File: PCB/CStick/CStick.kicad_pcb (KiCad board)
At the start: 2 copper layers, 39.1 x 31.5 mm, 6 parts, among them J1 Conn_01x04_Male, U1 Stickbox_Assembly

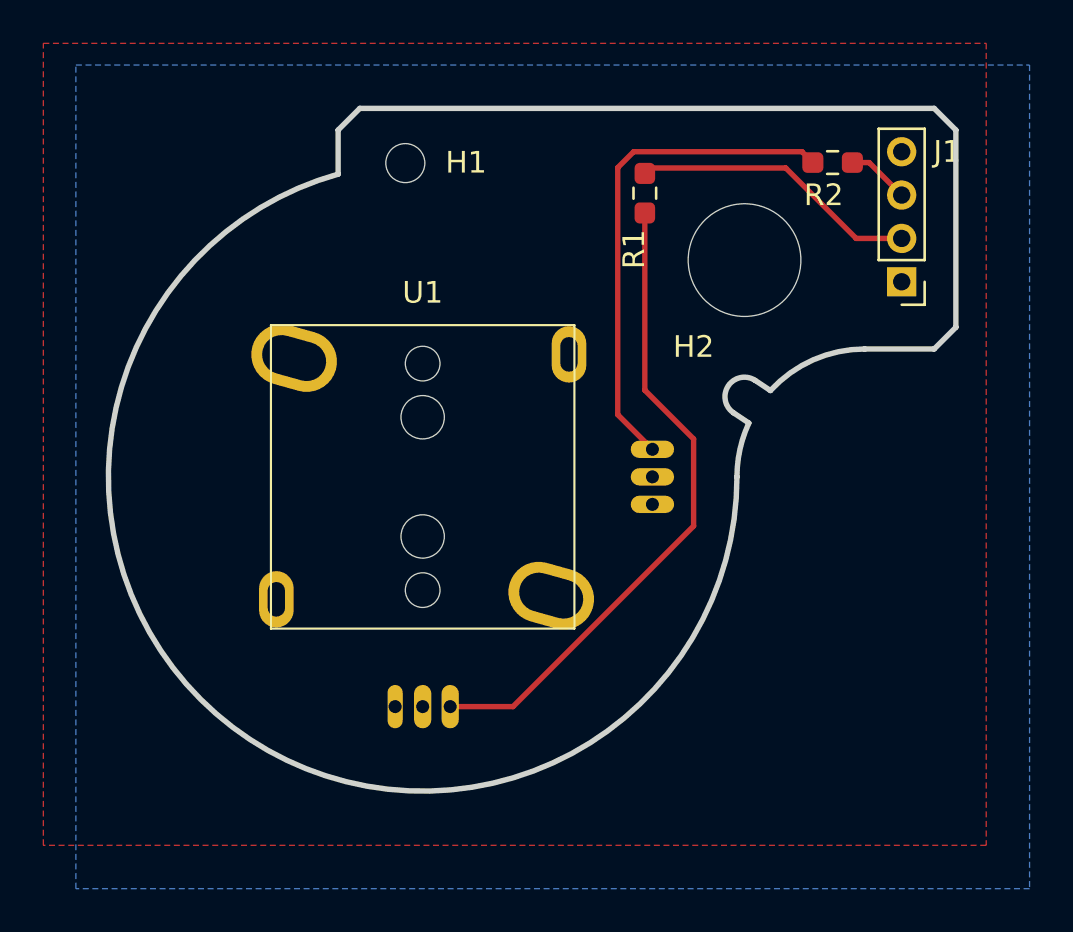
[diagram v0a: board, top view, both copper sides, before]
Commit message: Changed PCB folder structure to sperate Motherboard from Cstick board, updated the diode part number for JLC to one that is in stock
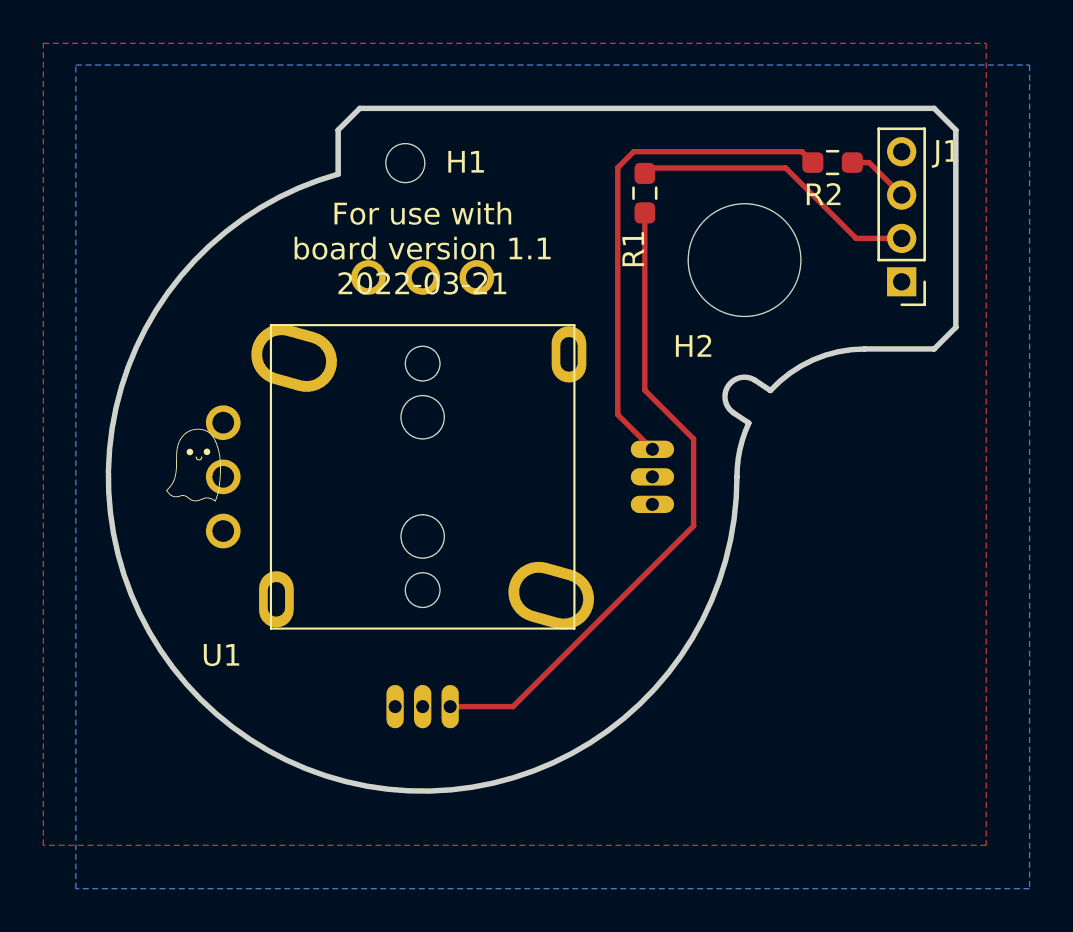
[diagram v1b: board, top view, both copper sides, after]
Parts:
- added G***: LOGO, Gamecube MB:Ghost Logo Small, F.Cu at (139.5, 99.5)
- U1: footprint Gamecube MB:GCC_Stickbox_Hall_Only -> Gamecube MB:GCC_Stickbox_2
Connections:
- net Net-(J1-Pad2) renamed /X_Conn
- net Net-(J1-Pad3) renamed /Y_Conn
- R1 pad 2: Net-(R1-Pad2) -> /X_Hall
- R2 pad 2: Net-(R2-Pad2) -> /Y_Hall
- U1 pad 3: Net-(R1-Pad2) -> /X_Hall
- U1 pad 6: Net-(R2-Pad2) -> /Y_Hall
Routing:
- net Net-(R1-Pad2): track 30.1 -> 0.00 mm
- net /X_Hall: track 0.00 -> 30.1 mm
- net Net-(R2-Pad2): track 23.2 -> 0.00 mm
- net /Y_Hall: track 0.00 -> 23.2 mm
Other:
- board text added: "For use with board version 1.1 2022-03-21"
